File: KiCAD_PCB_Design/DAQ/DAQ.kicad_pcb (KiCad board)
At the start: 2 copper layers, 100 x 99 mm, 130 parts, among them P1 SMA, P10 EXTRA_CONN_HEADERS, P11 Connection with FPGA, P12 ADC_STAT, P13 ADC_STAT, P14 ADC_STAT, P15 ADC_STAT, P16 ADC_STAT, P17 ADC_STAT, P18 ADC_STAT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

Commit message: VCO PCB design complete, ongoing LNA & PA ..
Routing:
- net (no net): track 0.00 -> 2.96 mm, vias 0 -> 71
- net GND: vias 23 -> 29
- added copper zone on B.Cu, net GND
- added copper zone on F.Cu, net GND

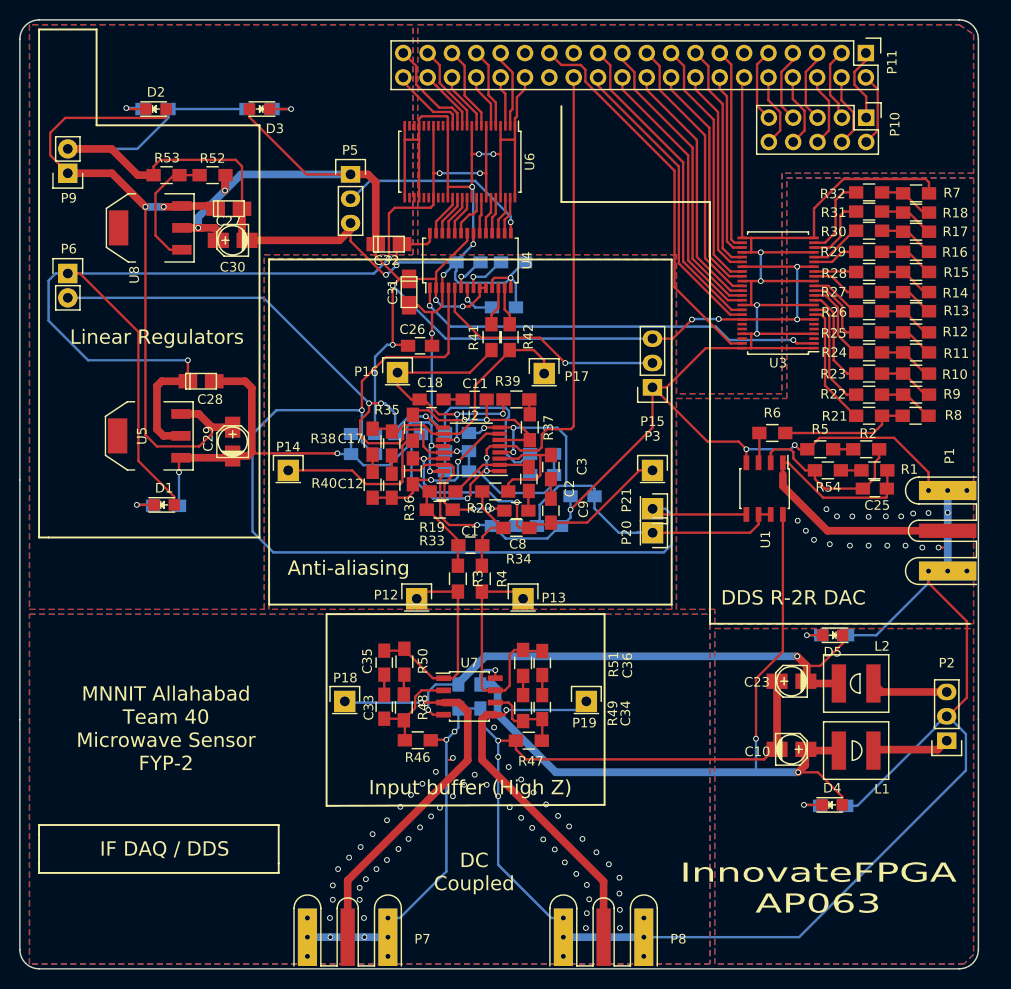
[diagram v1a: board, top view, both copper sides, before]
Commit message: All components made except antenna, Now verifying ..
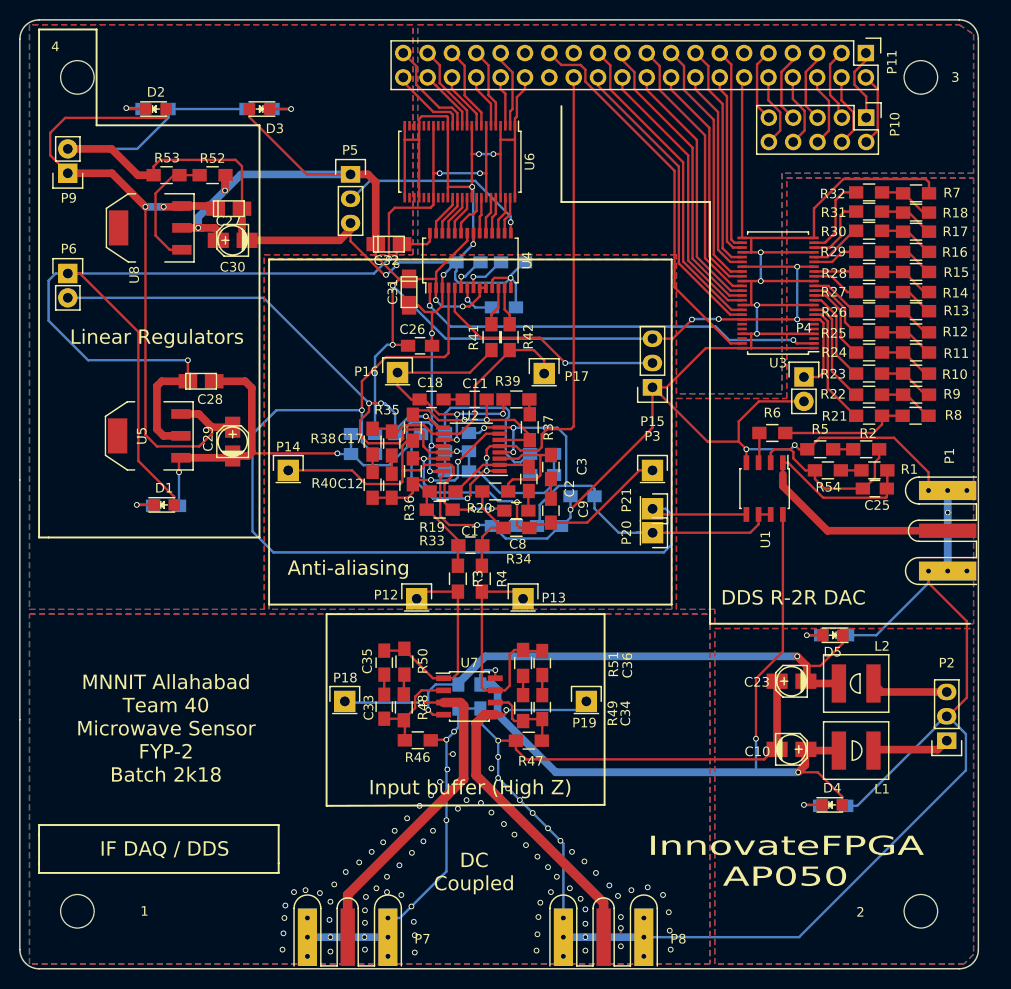
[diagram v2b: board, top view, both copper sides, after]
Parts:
- added 1: MountingHole_3-5mm, Mounting_Holes:MountingHole_3-5mm, F.Cu at (83.0, 153.0)
- added 2: MountingHole_3-5mm, Mounting_Holes:MountingHole_3-5mm, F.Cu at (171.0, 153.0)
- added 3: MountingHole_3-5mm, Mounting_Holes:MountingHole_3-5mm, F.Cu at (171.0, 66.0)
- added 4: MountingHole_3-5mm, Mounting_Holes:MountingHole_3-5mm, F.Cu at (83.0, 66.0)
- added P4: VCO_SUPPLY, Pin_Headers:Pin_Header_Straight_1x02, F.Cu at (158.8, 97.3)
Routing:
- net GND: track 690.9 -> 700.1 mm, vias 29 -> 38
- net VDD: track 153.1 -> 161.6 mm
- net (no net): track 2.96 -> 1.90 mm
- net /R2R_DATA_10: track 11.9 -> 11.3 mm
- net Net-(P19-Pad1): track 39.8 -> 40.4 mm
- net /R2R_DATA_07: track 7.55 -> 7.03 mm
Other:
- board text added: "InnovateFPGA AP050"
- board text added: "MNNIT Allahabad Team 40 Microwave Sensor FYP-2 Batch 2k18"
- board text removed: "InnovateFPGA AP063"
- board text removed: "MNNIT Allahabad Team 40 Microwave Sensor FYP-2"
